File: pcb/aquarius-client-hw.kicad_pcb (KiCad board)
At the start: 4 copper layers, 50 x 50 mm, 227 parts, among them J3 USB_C_USB2.0_16P, Q1 MMBT2222A, SW1 EVQ-Q2B02W, SW2 EVQ-Q2B02W, U1 ESP32-S3-WROOM-1-N8R2, U2 HDC1080, U3 LTR-303ALS-01, U4 USBLC6-2P6, U5 LM66200DRLR, U6 LM66200DRLR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

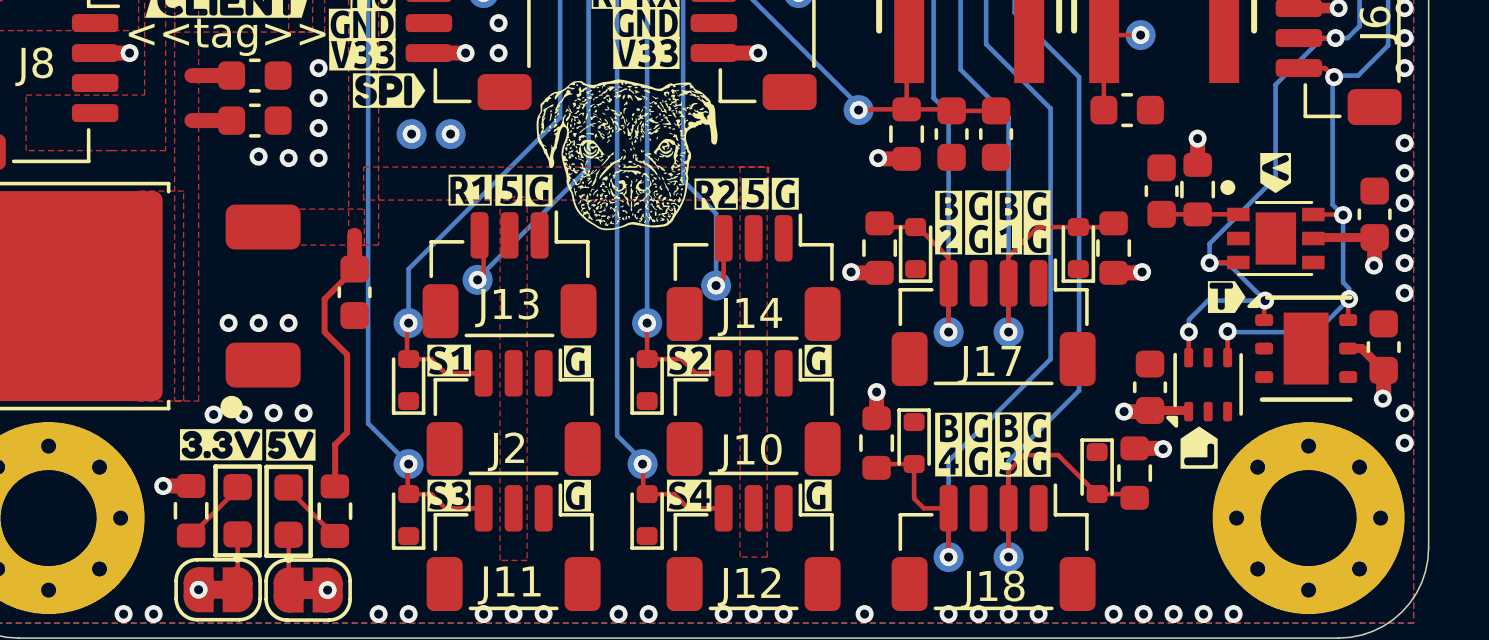
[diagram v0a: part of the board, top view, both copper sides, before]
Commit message: Updated LED footprint
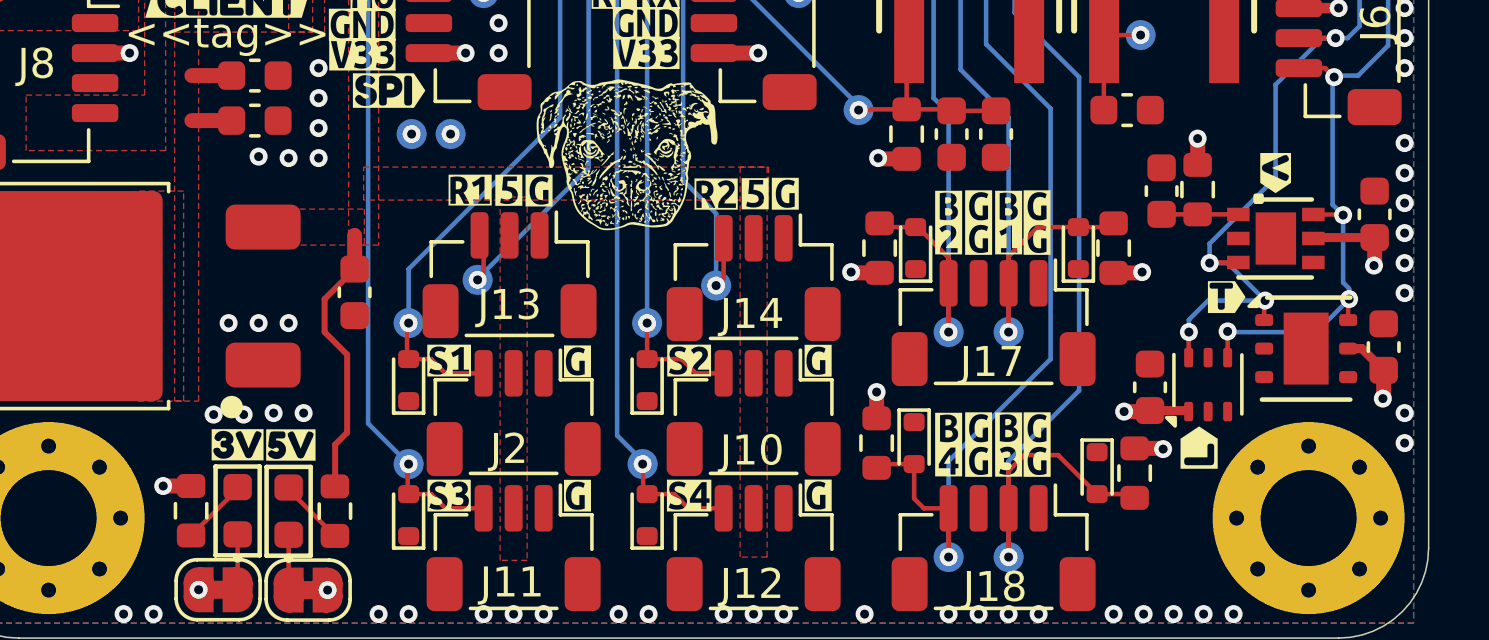
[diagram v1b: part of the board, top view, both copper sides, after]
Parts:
- removed kibuzzard-68BB9AFB: G***, kibuzzard-68BB9AFB
- added kibuzzard-690A7D58: G***, kibuzzard-690A7D58, F.Cu at (60.3, 103.6)
- D7, D8: footprint CRG Makes:LED_0603_1608Metric -> CRGM Passive:LED_0603_1608Metric
